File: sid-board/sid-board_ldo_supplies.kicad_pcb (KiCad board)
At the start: 2 copper layers, 42.8 x 68.8 mm, 13 parts, among them J1 ICM_CONN, J2 SID_CONN, J3 5V/GND, J4 3.3V/GND, J5 SPI, J6 UARTAB/IRQ, U1 SC16IS752IPW, U2 MCP1703A-3302_SOT223, U3 PCA82C250, U4 PCA82C250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

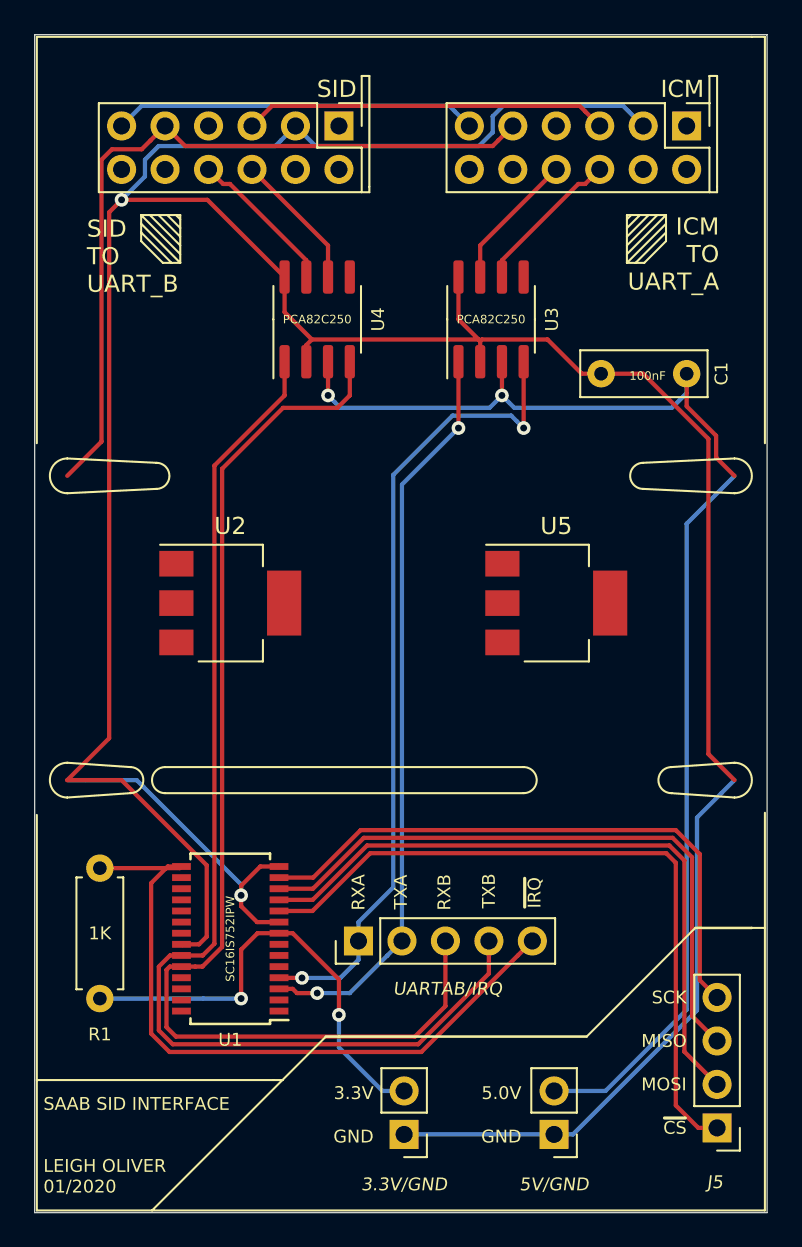
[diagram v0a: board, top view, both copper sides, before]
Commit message: Working on new mostly-SMD version, switched to independant LDOs, added oscillator circuit.
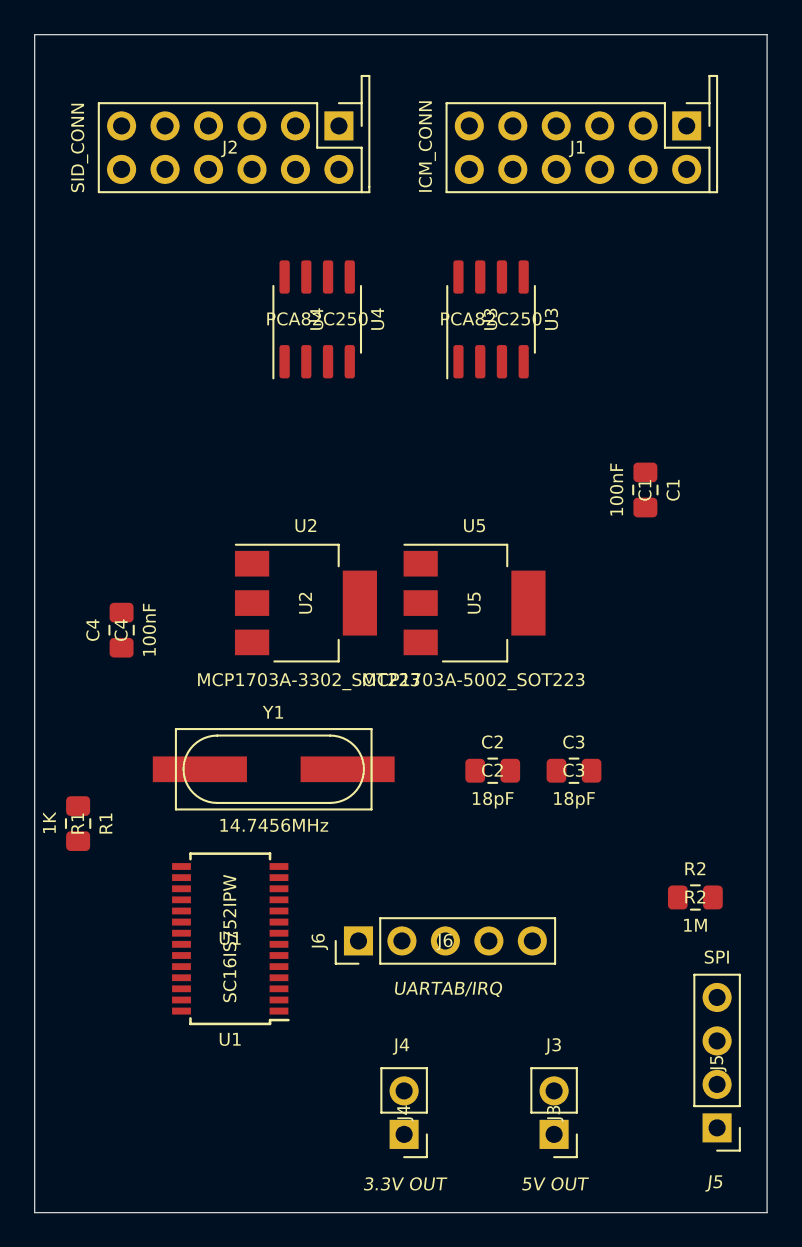
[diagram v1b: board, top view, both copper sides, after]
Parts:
- added C2: 18pF, Capacitor_SMD:C_0805_2012Metric_Pad1.15x1.40mm_HandSolder, F.Cu at (89.0, 102.6)
- added C3: 18pF, Capacitor_SMD:C_0805_2012Metric_Pad1.15x1.40mm_HandSolder, F.Cu at (93.7, 102.6)
- added C4: 100nF, Capacitor_SMD:C_0805_2012Metric_Pad1.15x1.40mm_HandSolder, F.Cu at (67.3, 94.4)
- added R2: 1M, Resistor_SMD:R_0805_2012Metric_Pad1.15x1.40mm_HandSolder, F.Cu at (100.8, 110.0)
- added Y1: 14.7456MHz, sid-board:Euroquarts 14.7456MHz Crystal ±30ppm SMD 2-Pin 12.4 x 4.5 x 4.2mm, F.Cu at (76.2, 102.5)
- C1: footprint Capacitor_THT:C_Rect_L7.2mm_W2.5mm_P5.00mm_FKS2_FKP2_MKS2_MKP2 -> Capacitor_SMD:C_0805_2012Metric_Pad1.15x1.40mm_HandSolder
- J3: value 5V/GND -> 5V OUT
- J4: value 3.3V/GND -> 3.3V OUT
- R1: footprint Resistor_THT:R_Axial_DIN0207_L6.3mm_D2.5mm_P7.62mm_Horizontal -> Resistor_SMD:R_0805_2012Metric_Pad1.15x1.40mm_HandSolder
- moved C1 7.21 mm to (97.9, 86.2), turned to 270 degrees
- moved U5 4.77 mm to (87.9, 92.8)
- moved U2 4.43 mm to (78.1, 92.8)
- moved R1 2.90 mm to (64.8, 105.7)
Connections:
- U1 pad 6: Net-(U1-Pad6) -> XTAL1
- U1 pad 7: Net-(U1-Pad7) -> XTAL2
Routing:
- net GND: track 209.9 -> 0.00 mm, vias 2 -> 0
- net VDD_5V: track 76.5 -> 0.00 mm, vias 2 -> 0
- net Net-(J6-Pad3): track 67.4 -> 0.00 mm
- net Net-(J6-Pad4): track 66.5 -> 0.00 mm
- net Net-(J6-Pad1): track 47.5 -> 0.00 mm, vias 2 -> 0
- net VIN: track 45.1 -> 0.00 mm
- net Net-(J6-Pad2): track 43.8 -> 0.00 mm, vias 2 -> 0
- net Net-(J5-Pad1): track 41.9 -> 0.00 mm
- net Net-(J6-Pad5): track 41.2 -> 0.00 mm
- net Net-(J5-Pad2): track 39.2 -> 0.00 mm
- net Net-(J5-Pad3): track 37.2 -> 0.00 mm
- net Net-(J5-Pad4): track 35.1 -> 0.00 mm
- net VDD_3.3V: track 27.2 -> 0.00 mm, vias 2 -> 0
- net Net-(J1-Pad6): track 21.3 -> 0.00 mm
- net Net-(J1-Pad3): track 21.3 -> 0.00 mm
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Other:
- board text removed: "3.3V"
- board text removed: "5.0V"
- board text removed: "GND"
- board text removed: "ICM"
- board text removed: "ICM TO UART_A"
- board text removed: "MISO"
- board text removed: "MOSI"
- board text removed: "RXA"
- board text removed: "RXB"
- board text removed: "SAAB SID INTERFACE LEIGH OLIVER 01/2020"
- board text removed: "SCK"
- board text removed: "SID"
- board text removed: "SID TO UART_B"
- board text removed: "TXA"
- board text removed: "TXB"
- board text removed: "~CS"
- board text removed: "~IRQ"

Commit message: Re-did PCB layout, signifcantly smaller now.
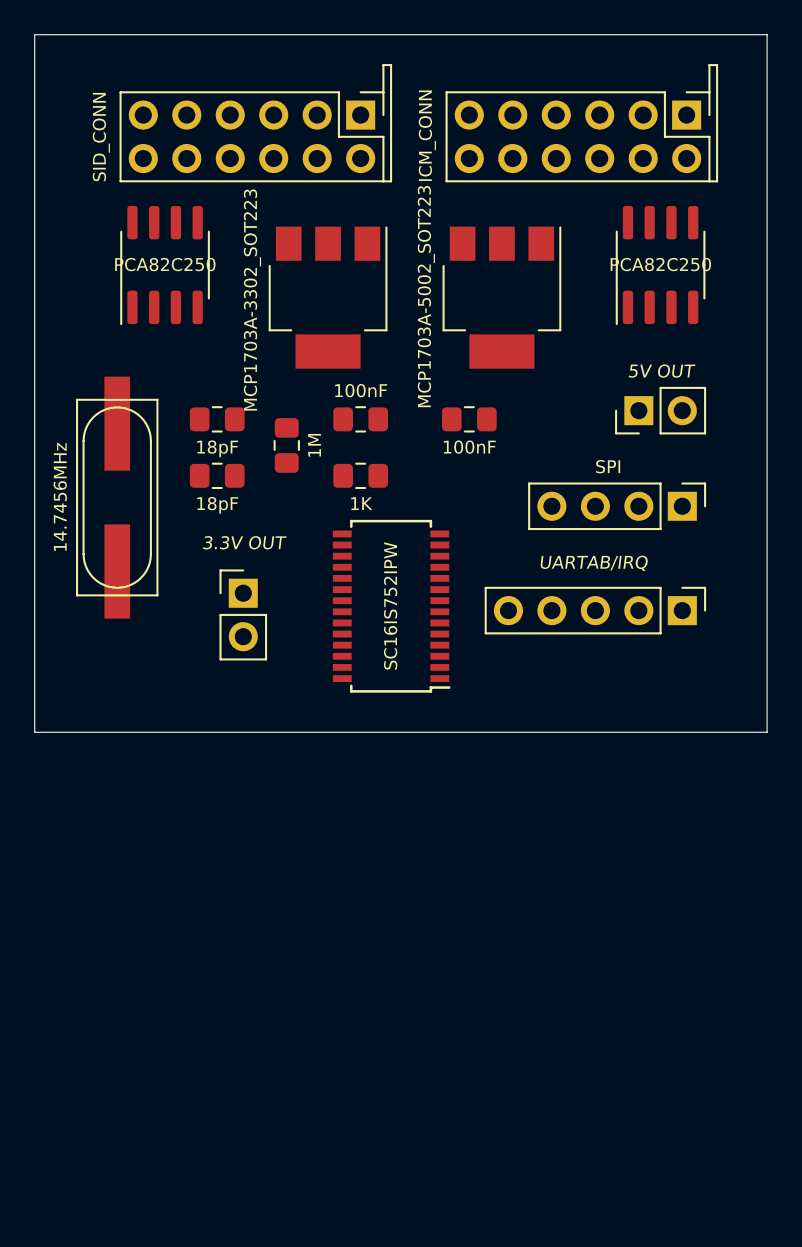
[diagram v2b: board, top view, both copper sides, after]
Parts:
- moved J3 42.6 mm to (97.5, 81.5), turned to 90 degrees
- moved J5 36.4 mm to (100.1, 87.1), turned to 270 degrees
- moved R2 35.6 mm to (77.0, 83.6), turned to 90 degrees
- moved J4 33.0 mm to (74.4, 92.2), turned to 0 degrees
- moved C3 27.0 mm to (72.9, 85.3)
- moved J6 27.0 mm to (100.1, 93.2), turned to 270 degrees
- moved R1 26.2 mm to (81.3, 85.3), turned to 0 degrees
- moved C2 26.1 mm to (72.9, 82.0)
- moved U1 21.6 mm to (83.1, 93.0)
- moved C4 18.6 mm to (81.3, 82.0), turned to 180 degrees
- moved Y1 18.3 mm to (67.1, 86.6), turned to 270 degrees
- moved U5 17.9 mm to (89.5, 74.9), turned to 270 degrees
- moved U2 17.9 mm to (79.4, 74.9), turned to 270 degrees
- moved C1 11.1 mm to (87.6, 82.0), turned to 0 degrees
- moved U3 10.4 mm to (98.8, 73.0)
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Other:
- board size 42.8 x 68.8 mm -> 42.8 x 40.8 mm

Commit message: Layout and edgecut tweaks.
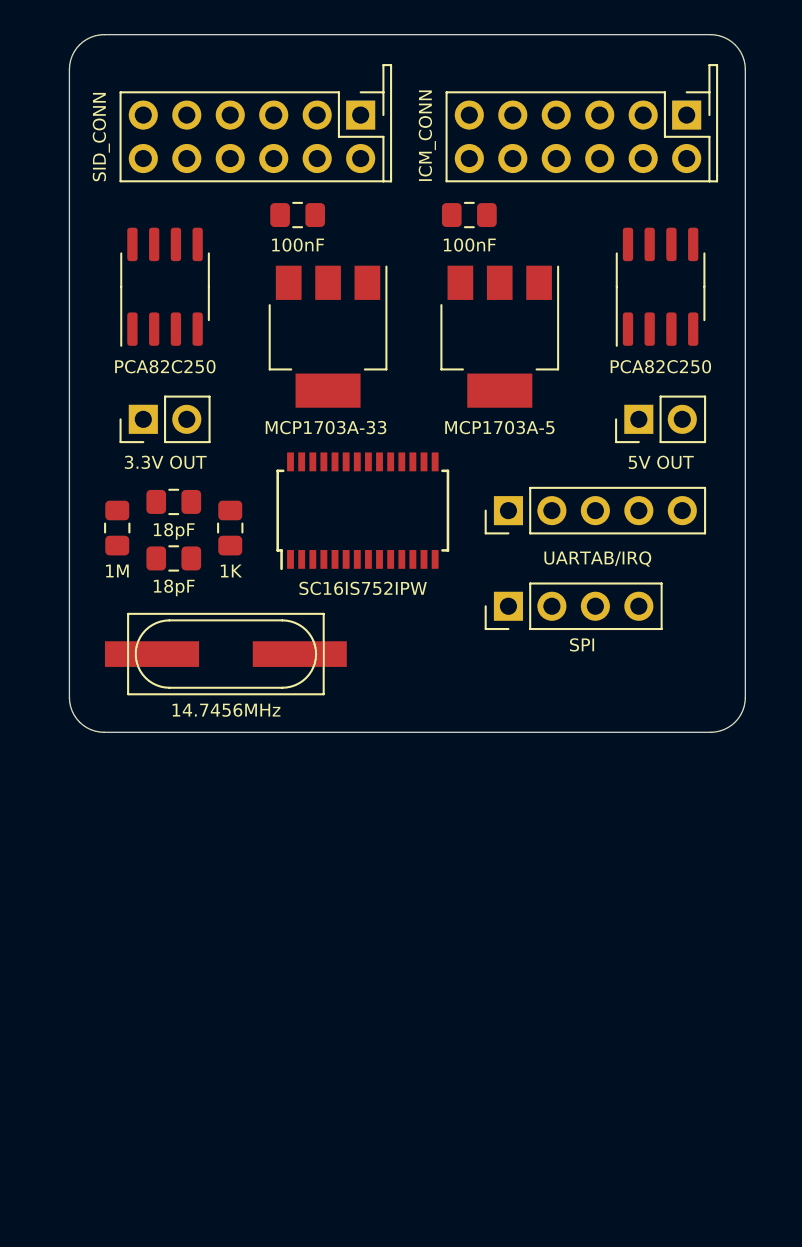
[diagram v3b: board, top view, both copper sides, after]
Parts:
- U2: value MCP1703A-3302_SOT223 -> MCP1703A-33
- U5: value MCP1703A-5002_SOT223 -> MCP1703A-5
- moved C4 12.5 mm to (77.6, 70.1), turned to 0 degrees
- moved C1 11.9 mm to (87.6, 70.1)
- moved J4 11.7 mm to (68.6, 82.0), turned to 90 degrees
- moved J5 11.7 mm to (89.9, 93.0), turned to 90 degrees
- moved J6 11.7 mm to (89.9, 87.4), turned to 90 degrees
- moved Y1 11.1 mm to (73.4, 95.8), turned to 0 degrees
- moved R2 11.0 mm to (67.1, 88.4)
- moved R1 8.21 mm to (73.7, 88.4), turned to 90 degrees
- moved U1 5.83 mm to (81.4, 87.4), turned to 90 degrees
- moved C3 5.45 mm to (70.4, 90.2)
- moved C2 5.45 mm to (70.4, 86.9)
- moved U5 2.29 mm to (89.4, 77.2)
- moved U2 2.29 mm to (79.4, 77.2)
- moved U3 1.27 mm to (98.8, 74.3)
- moved U4 1.27 mm to (69.8, 74.3)
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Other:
- board size 42.8 x 40.8 mm -> 39.5 x 40.8 mm

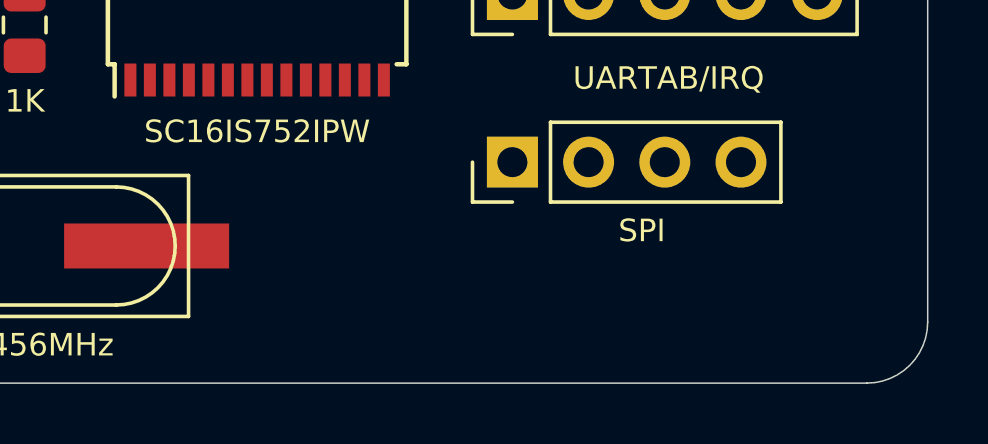
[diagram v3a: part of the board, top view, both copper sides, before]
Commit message: Added 3d files for proper female sockets, havn't placed yet. Added text.
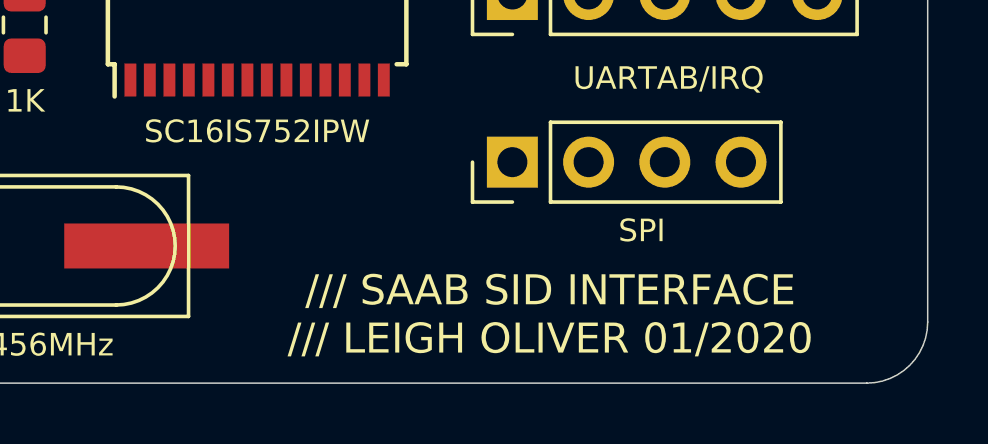
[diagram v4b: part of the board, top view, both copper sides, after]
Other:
- board text added: "/// SAAB SID INTERFACE /// LEIGH OLIVER 01/2020"

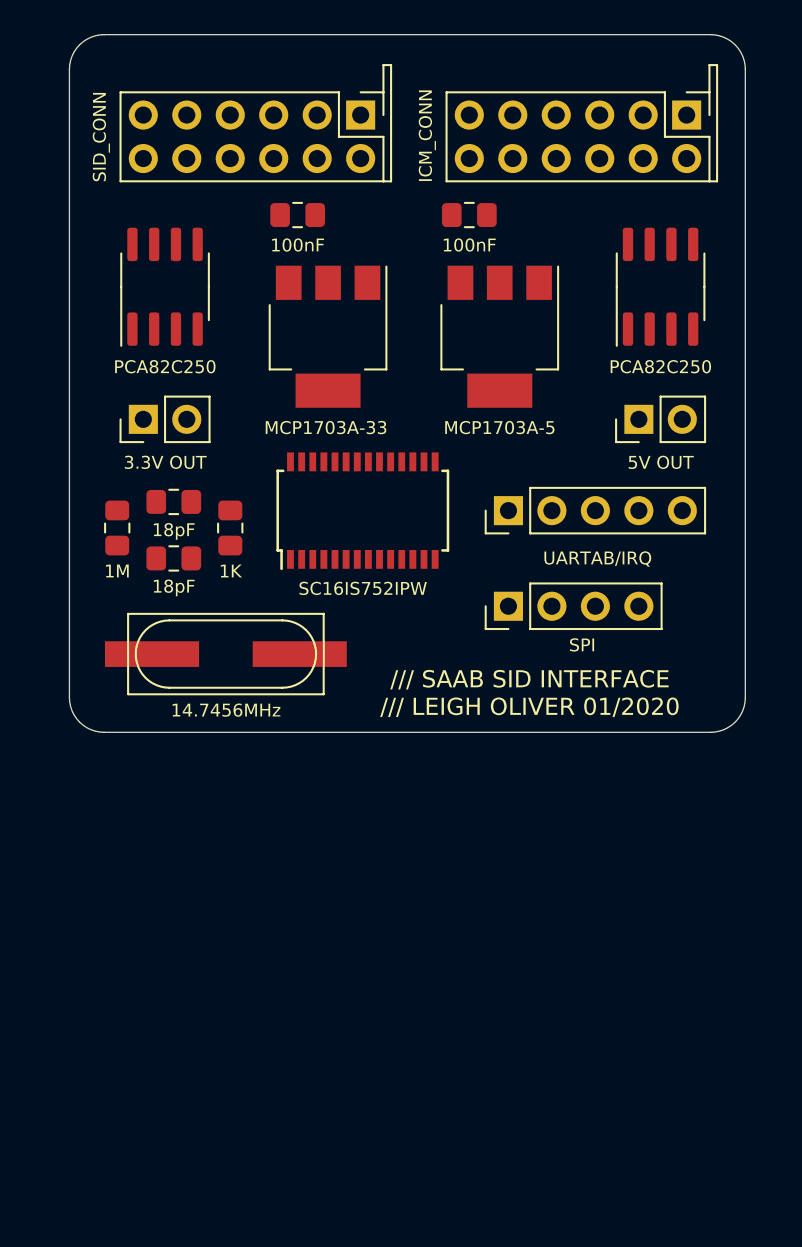
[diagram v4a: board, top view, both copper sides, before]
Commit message: Autorouted with Freerouting
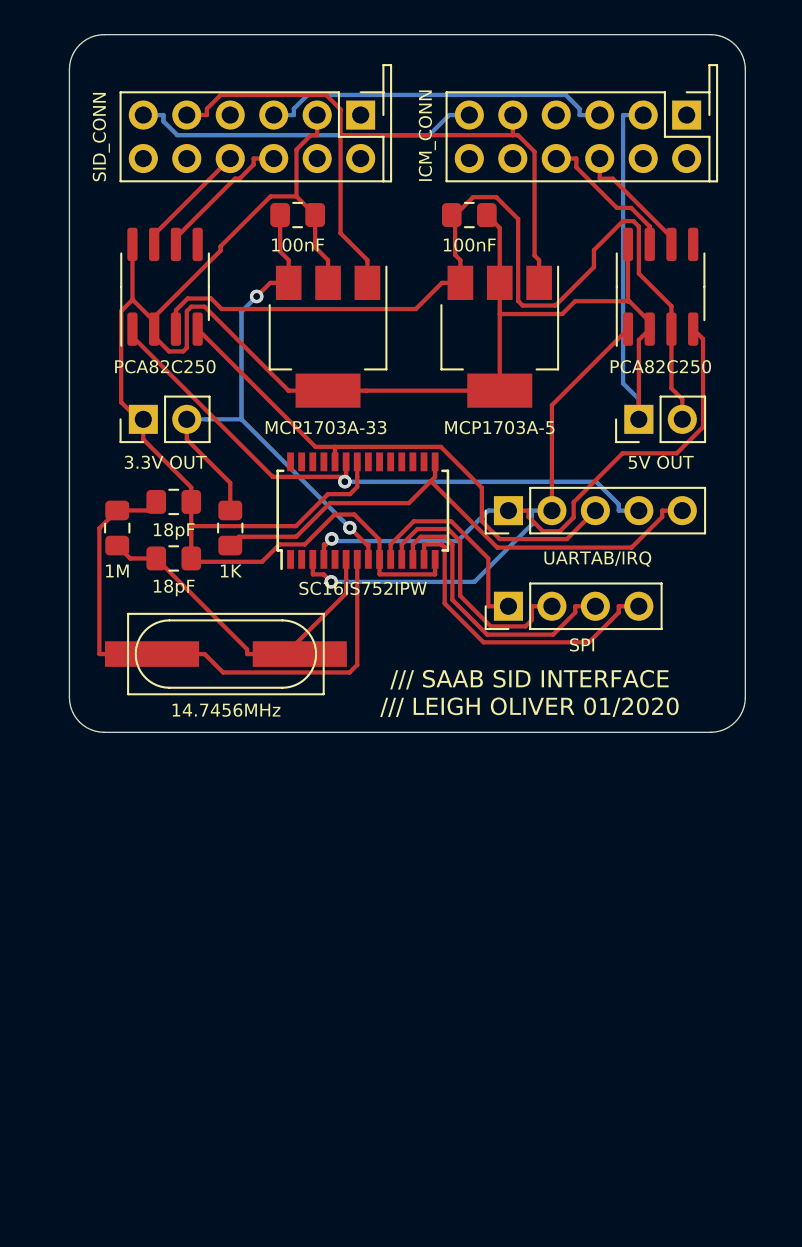
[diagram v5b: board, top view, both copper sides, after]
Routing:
- net GND: track 0.00 -> 151.0 mm
- net VDD_5V: track 0.00 -> 54.9 mm
- net VIN: track 0.00 -> 41.5 mm
- net Net-(J6-Pad4): track 0.00 -> 35.6 mm, vias 0 -> 1
- net VDD_3.3V: track 0.00 -> 34.8 mm, vias 0 -> 2
- net Net-(J6-Pad1): track 0.00 -> 33.7 mm, vias 0 -> 1
- net XTAL2: track 0.00 -> 33.2 mm
- net Net-(J6-Pad5): track 0.00 -> 31.9 mm
- net Net-(J6-Pad3): track 0.00 -> 31.0 mm
- net Net-(J6-Pad2): track 0.00 -> 29.7 mm, vias 0 -> 1
- net XTAL1: track 0.00 -> 20.5 mm
- net Net-(J1-Pad3): track 0.00 -> 20.5 mm
- net Net-(J1-Pad6): track 0.00 -> 20.2 mm
- net Net-(J5-Pad4): track 0.00 -> 18.8 mm
- net Net-(J5-Pad3): track 0.00 -> 16.9 mm
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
